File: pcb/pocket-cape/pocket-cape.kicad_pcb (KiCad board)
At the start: 4 copper layers, 49 x 32.1 mm, 27 parts, among them J1 Sync1, J10 Display, J11 USB1, J2 12..16V, J3 Sync2, J4 Sled, J5 Laser1, J6 PM1, J7 PM2, J8 Laser2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

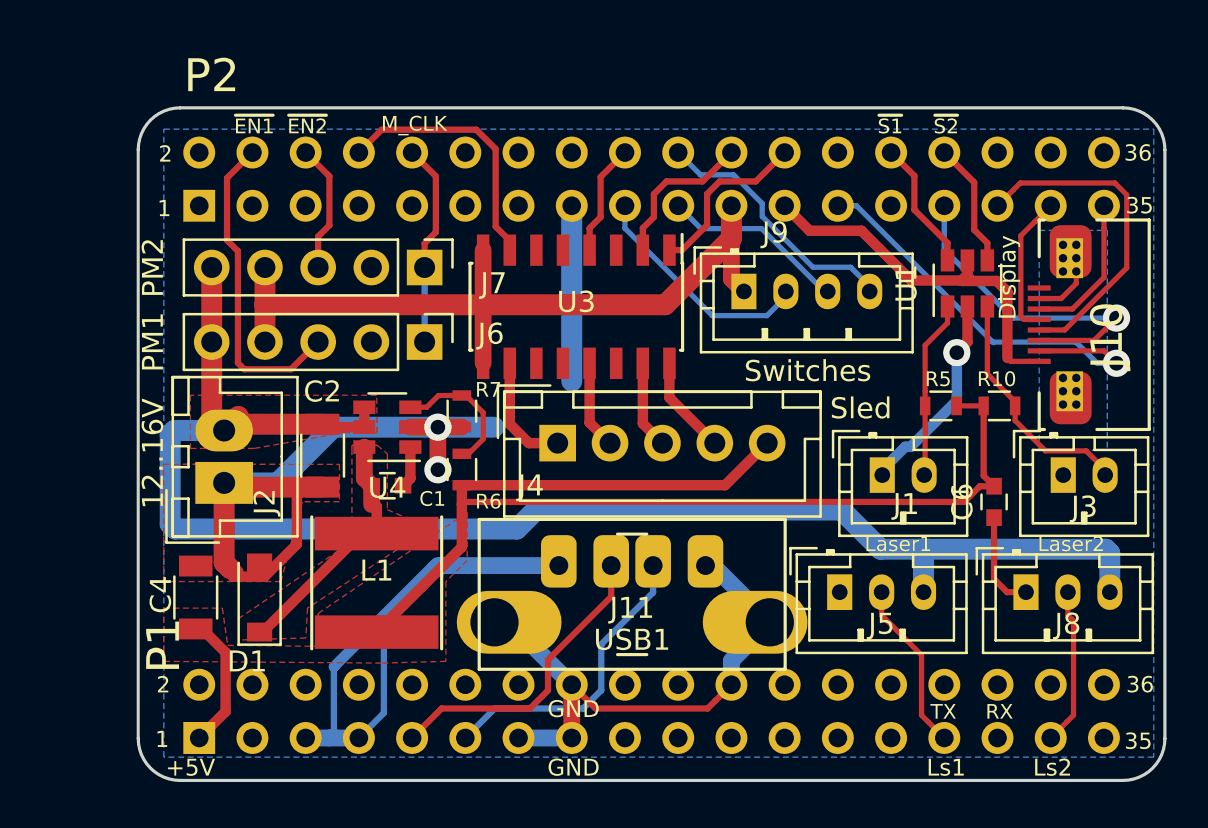
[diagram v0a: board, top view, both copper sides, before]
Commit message: Add a capacitor in the stepper driver vicinity.
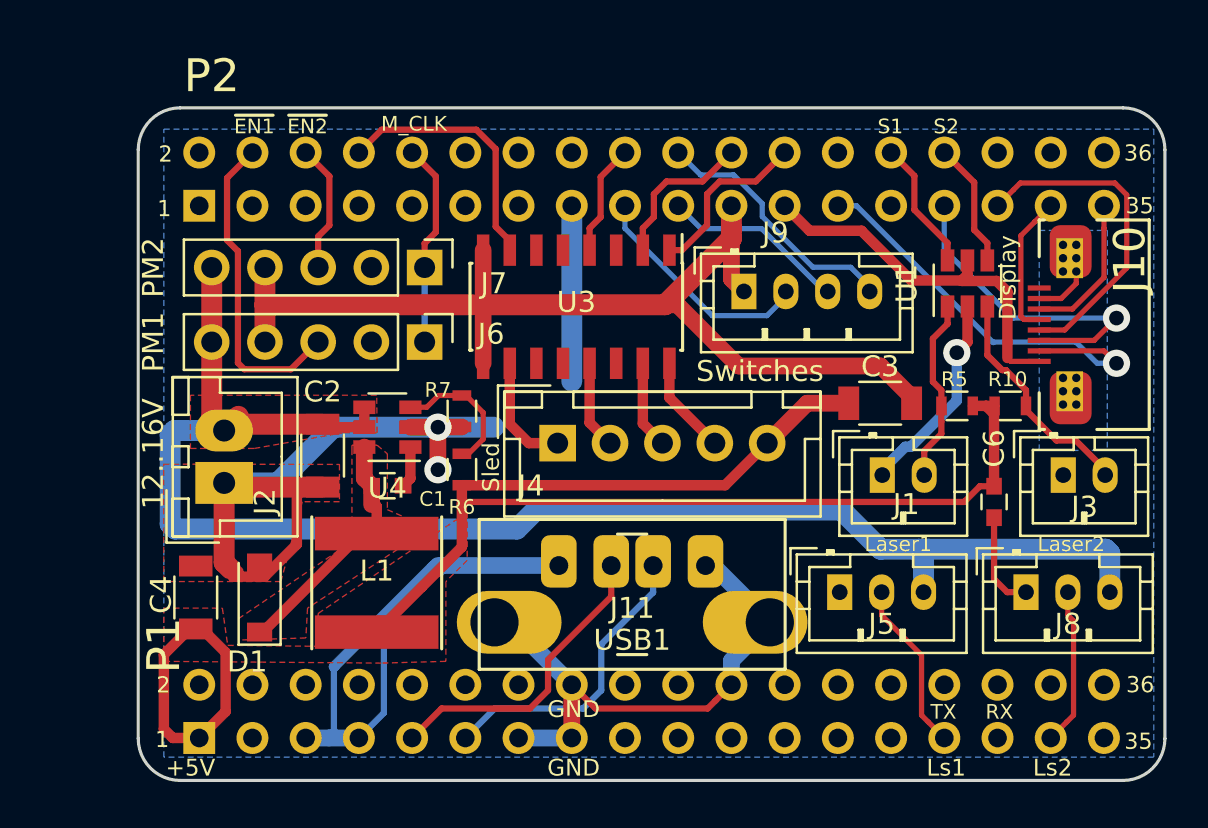
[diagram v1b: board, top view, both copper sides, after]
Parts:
- added C3: 22u, Capacitors_SMD:C_1206, F.Cu at (159.4, 103.0)
- moved R5 0.77 mm to (163.1, 103.1)
- moved REF*** 0.52 mm to (148.5, 97.8)
- moved R10 0.52 mm to (165.6, 103.1)
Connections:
- J10 pad 8: Net-(J10-Pad8) -> (no net)
- J6 pad 2: (no net) -> Net-(J6-Pad2)
- J7 pad 2: (no net) -> Net-(J7-Pad2)
- P1 pad 10: (no net) -> /(U1.B13)SPI0.MISO
- P1 pad 12: (no net) -> /(U1.B14)SPI0.MOSI
- P1 pad 14: Net-(P1-Pad14) -> (no net)
- P1 pad 17: (no net) -> /(U1.B9)VREF-
- P1 pad 18: (no net) -> /(U1.B7)VREF+
- P1 pad 19: (no net) -> /(U1.A8)AIN0~1.8V
- P1 pad 2: (no net) -> /(U1.F2)AIN6~3.3V
- P1 pad 20: (no net) -> /(U1.B4)PRU-0.16
- P1 pad 21: (no net) -> /(U1.B8)AIN1~1.8V
- P1 pad 23: (no net) -> /(U1.B6)AIN2~1.8V
- P1 pad 24: Net-(P1-Pad24) -> (no net)
- P1 pad 25: (no net) -> /(U1.C6)AIN3~1.8V
- P1 pad 26: (no net) -> /(U1.B10)I2C2.SDA
- P1 pad 27: (no net) -> /(U1.C7)AIN4~1.8V
- P1 pad 28: (no net) -> /(U1.A10)I2C2.SCL
- P1 pad 3: (no net) -> /(U1.M14)USB1.DRVVBUS
- P1 pad 30: (no net) -> /(U1.B12)UART0.TX
- P1 pad 31: (no net) -> /(U1.A3)PRU-0.4
- P1 pad 32: (no net) -> /(U1.A12)UART0.RX
- P1 pad 34: (no net) -> /(U1.R5)GPIO-0.26
- P1 pad 35: (no net) -> /(U1.F1)
- P1 pad 36: (no net) -> /(U1.A1)PWM0A
- P1 pad 4: (no net) -> /(U1.E1)
- P1 pad 6: (no net) -> /(U1.A14)SPI0.CS
- P1 pad 8: (no net) -> /(U1.A13)SPI0.CLK
- P2 pad 1: (no net) -> /(U1.P12)PWM1A
- P2 pad 11: (no net) -> /(U1.A11)I2C1.SDA
- P2 pad 12: (no net) -> /(U1.T11)PWR.BTN
- P2 pad 13: (no net) -> SYS_5V
- P2 pad 14: (no net) -> VIN.BAT
- P2 pad 16: (no net) -> /BAT.TEMP
- P2 pad 2: (no net) -> /(U1.T16)
- P2 pad 26: (no net) -> /(U1.R11)RESET#
- P2 pad 27: (no net) -> /(U1.C12)SPI1.MISO
- P2 pad 3: (no net) -> /(U1.P5)GPIO-0.23
- P2 pad 32: (no net) -> /(U1.B2)PRU-0.2
- P2 pad 34: (no net) -> /(U1.B3)PRU-0.5
- P2 pad 36: (no net) -> /(U1.N13)AIN7~1.8V
- P2 pad 5: (no net) -> /(U1.P15)UART4.RX
- P2 pad 7: (no net) -> /(U1.R16)UART4.TX
- P2 pad 9: (no net) -> /(U1.B11)I2C1.SCL
- U3 pad 11: Net-(U3-Pad11) -> (no net)
- U3 pad 12: Net-(U3-Pad12) -> (no net)
- U3 pad 14: Net-(U3-Pad14) -> (no net)
- U3 pad 3: Net-(U3-Pad3) -> (no net)
- U3 pad 5: Net-(U3-Pad5) -> (no net)
- U3 pad 6: Net-(U3-Pad6) -> (no net)
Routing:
- net GND: track 127.6 -> 141.8 mm
- net VDD_5V: track 64.3 -> 76.1 mm
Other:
- net class Default: clearance 0.18 -> 0.4
- rule trace_clearance: 0.18 -> 0.4
- board text added: "S1"
- board text added: "S2"
- board text removed: "~S1"
- board text removed: "~S2"

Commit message: Improve silkscreen.
o Label signals directly on header for easier measurements.
o Arrange partially obstructed component labels.
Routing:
- net +12V: track 75.3 -> 83.3 mm
- net GND: track 141.8 -> 145.3 mm
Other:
- board text added: "3.3V"
- board text added: "B1"
- board text added: "B2"
- board text added: "B3"
- board text added: "CLK"
- board text added: "DC"
- board text added: "HS1"
- board text added: "HS2"
- board text added: "MOSI"
- board text added: "RST"
- board text added: "~CS"
- board text removed: "S1"
- board text removed: "S2"
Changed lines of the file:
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@@
   (general
     (thickness 1.6)
-    (drawings 443)
-    (tracks 316)
+    (drawings 453)
+    (tracks 320)
     (zones 0)
     (modules 28)
@@
   )
   (setup
-    (last_trace_width 0.5)
+    (last_trace_width 1)
     (user_trace_width 0.25)
     (user_trace_width 0.3)
@@
     (pad_to_mask_clearance 0.0254)
     (aux_axis_origin 0 0)
-    (visible_elements FFFFEF7F)
+    (visible_elements FFFDEF7F)
     (pcbplotparams
       (layerselection 0x010fc_fffffff9)
@@
       (effects (font (size 0.7 0.7) (thickness 0.15)))
     )
-    (fp_text value C (at 0 1.5 180) (layer F.Fab)
+    (fp_text value C (at 0 0 180) (layer F.Fab)
       (effects (font (size 1 1) (thickness 0.15)))
     )
@@
       (effects (font (size 1 1) (thickness 0.15)))
     )
-    (fp_text value 10u (at 0 2 270) (layer F.Fab)
+    (fp_text value 10u (at 0.037 -0.042 270) (layer F.Fab)
       (effects (font (size 1 1) (thickness 0.15)))
     )
@@
     (fp_line (start 1.6 0.8) (end -1.6 0.8) (layer F.Fab) (width 0.1))
     (fp_line (start -1.6 0.8) (end -1.6 -0.8) (layer F.Fab) (width 0.1))
-    (fp_text user %R (at 0 -1.75 270) (layer F.Fab)
+    (fp_text user %R (at 2.577 0.212 270) (layer F.Fab)
       (effects (font (size 1 1) (thickness 0.15)))
     )
@@
       (effects (font (size 1 1) (thickness 0.15)))
     )
-    (fp_text value 22u (at 0 2 90) (layer F.Fab)
+    (fp_text value 22u (at 0 0 90) (layer F.Fab)
       (effects (font (size 1 1) (thickness 0.15)))
     )
@@
       (effects (font (size 1 1) (thickness 0.15)))
     )
-    (fp_text value D (at 0 2.1 90) (layer F.Fab)
+    (fp_text value D (at 0.762 0.127 90) (layer F.Fab)
       (effects (font (size 1 1) (thickness 0.15)))
     )
-    (fp_text user %R (at 0 -2 90) (layer F.Fab)
+    (fp_text user %R (at -1.27 1.651 90) (layer F.Fab)
       (effects (font (size 1 1) (thickness 0.15)))
     )
@@
       (effects (font (size 0.7 0.7) (thickness 0.15)))
     )
-    (fp_text value R (at 0 1.5 90) (layer F.Fab)
+    (fp_text value R (at 0.115 1.397 90) (layer F.Fab)
       (effects (font (size 1 1) (thickness 0.15)))
     )
@@
       (effects (font (size 0.7 0.7) (thickness 0.15)))
     )
-    (fp_text value R (at 0 1.5 270) (layer F.Fab)
+    (fp_text value R (at -0.127 -1.397 270) (layer F.Fab)
       (effects (font (size 1 1) (thickness 0.15)))
     )
-    (fp_text user %R (at 0.065999 2.3475 270) (layer F.Fab)
+    (fp_text user %R (at 0 0 270) (layer F.Fab)
       (effects (font (size 0.4 0.4) (thickness 0.075)))
     )
@@
     (tags SOT-23-6)
     (attr smd)
-    (fp_text reference U4 (at 0 -2.9 180) (layer F.SilkS)
+    (fp_text reference U4 (at 0.127 2.159 180) (layer F.SilkS)
       (effects (font (size 1 1) (thickness 0.15)))
     )
@@
       (effects (font (size 0.7 0.7) (thickness 0.12)))
     )
-    (fp_text value 100k (at 0 1.5) (layer F.Fab)
+    (fp_text value 100k (at -0.266 -1.27) (layer F.Fab)
       (effects (font (size 1 1) (thickness 0.15)))
     )
@@
       (effects (font (size 0.7 0.7) (thickness 0.12)))
     )
-    (fp_text value 100k (at 0.762 1.143 180) (layer F.Fab)
+    (fp_text value 100k (at -1.131 1.27 180) (layer F.Fab)
       (effects (font (size 1 1) (thickness 0.15)))
     )
@@
       (effects (font (size 1 1) (thickness 0.15)))
     )
-    (fp_text value 4u7 (at 0 4.5 270) (layer F.Fab)
+    (fp_text value 4u7 (at 0.19 -2.159 270) (layer F.Fab)
       (effects (font (size 1 1) (thickness 0.15)))
     )
@@
       (effects (font (size 1 1) (thickness 0.15)))
     )
-    (fp_text value 100n (at 0 1.5 90) (layer F.Fab)
+    (fp_text value 100n (at 0.139 1.143 90) (layer F.Fab)
       (effects (font (size 1 1) (thickness 0.15)))
     )
-    (fp_text user %R (at 0 -1.5 90) (layer F.Fab)
+    (fp_text user %R (at 1.917 0.127 90) (layer F.Fab)
       (effects (font (size 1 1) (thickness 0.15)))
     )
@@
     (tags "SOIC 1.27")
     (attr smd)
-    (fp_text reference U3 (at -0.221 0) (layer F.SilkS)
+    (fp_text reference U3 (at -3.269 -6.223) (layer F.SilkS)
       (effects (font (size 1 1) (thickness 0.15)))
     )
@@
     (descr "JST PH series connector, B4B-PH-K, top entry type, through hole, Datasheet: http://www.jst-mfg.com/product/pdf/eng/ePH.pdf")
     (tags "connector jst ph")
-    (fp_text reference J9 (at 1.5 -2.8) (layer F.SilkS)
+    (fp_text reference J9 (at 5 1.8) (layer F.SilkS)
       (effects (font (size 1 1) (thickness 0.15)))
     )
@@
       (effects (font (size 1 1) (thickness 0.15)))
     )
-    (fp_text value Sync1 (at 1 3.8) (layer F.Fab)
+    (fp_text value Sync1 (at 1.143 2.413) (layer F.Fab)
       (effects (font (size 1 1) (thickness 0.15)))
     )
@@
       (effects (font (size 1 1) (thickness 0.15)))
     )
-    (fp_text value Sync2 (at 1 3.8) (layer F.Fab)
+    (fp_text value Sync2 (at 1.143 2.413) (layer F.Fab)
       (effects (font (size 1 1) (thickness 0.15)))
     )
@@
     (tags SOT-23-6)
     (attr smd)
-    (fp_text reference U1 (at 0 -2.9 90) (layer F.SilkS)
+    (fp_text reference U1 (at -2.794 1.143 180) (layer F.SilkS)
       (effects (font (size 1 1) (thickness 0.15)))
     )
-    (fp_text value 74LVC2G14GV (at 0 2.9 90) (layer F.Fab)
+    (fp_text value 74LVC2G14GV (at 1.905 -0.635 180) (layer F.Fab)
       (effects (font (size 1 1) (thickness 0.15)))
     )
@@
       (effects (font (size 1 1) (thickness 0.15)))
     )
-    (fp_text value 22u (at 0 2) (layer F.Fab)
+    (fp_text value 22u (at 0.103 0) (layer F.Fab)
       (effects (font (size 1 1) (thickness 0.15)))
     )
@@
     )
   )
+  (gr_text 3.3V (at 142.367 117.729) (layer F.SilkS)
+    (effects (font (size 0.6 0.6) (thickness 0.12)))
+  )
+  (gr_text 3.3V (at 154.94 92.329) (layer F.SilkS)
+    (effects (font (size 0.6 0.6) (thickness 0.12)))
+  )
+  (gr_text "MOSI\n\n" (at 157.48 92.964) (layer F.SilkS)
+    (effects (font (size 0.7 0.7) (thickness 0.12)))
+  )
+  (gr_text CLK (at 162.56 92.329) (layer F.SilkS)
+    (effects (font (size 0.7 0.7) (thickness 0.12)))
+  )
+  (gr_text ~CS (at 164.973 92.456) (layer F.SilkS)
+    (effects (font (size 0.6 0.6) (thickness 0.12)))
+  )
+  (gr_text DC (at 167.513 92.329) (layer F.SilkS)
+    (effects (font (size 0.7 0.7) (thickness 0.12)))
+  )
+  (gr_text RST (at 170.053 92.329) (layer F.SilkS)
+    (effects (font (size 0.7 0.7) (thickness 0.12)))
+  )
+  (gr_text B1 (at 147.193 92.456) (layer F.SilkS)
+    (effects (font (size 0.7 0.7) (thickness 0.15)))
+  )
+  (gr_text B2 (at 149.86 92.329) (layer F.SilkS)
+    (effects (font (size 0.7 0.7) (thickness 0.15)))
+  )
+  (gr_text B3 (at 149.86 89.789) (layer F.SilkS)
+    (effects (font (size 0.7 0.7) (thickness 0.15)))
+  )
   (gr_arc (start 171 90.9) (end 173 90.9) (angle -90) (layer Edge.Cuts) (width 0.15))
   (gr_arc (start 171 119) (end 171 121) (angle -90) (layer Edge.Cuts) (width 0.15))
@@
     (effects (font (size 0.8 0.8) (thickness 0.15)))
   )
-  (gr_text S1 (at 159.893 89.789) (layer F.SilkS)
+  (gr_text HS1 (at 159.893 89.789) (layer F.SilkS)
     (effects (font (size 0.7 0.7) (thickness 0.15)))
   )
-  (gr_text S2 (at 162.56 89.789) (layer F.SilkS)
+  (gr_text HS2 (at 162.56 89.789) (layer F.SilkS)
     (effects (font (size 0.7 0.7) (thickness 0.15)))
   )
@@
     (effects (font (size 0.0475 0.0475) (thickness 0.004)) (justify left bottom))
   )
+  (segment (start 130.048 96.52) (end 130.048 100.076) (width 1) (layer Bottom) (net 1))
   (segment (start 152.654 101.219) (end 159.431 101.219) (width 0.8) (layer Top) (net 1))
   (segment (start 159.431 101.219) (end 160.909 102.697) (width 0.8) (layer Top) (net 1))
@@
   (segment (start 136.99 105.09) (end 136.99 106.584) (width 0.5) (layer Top) (net 4))
   (segment (start 136.99 106.584) (end 136.64 106.934) (width 0.5) (layer Top) (net 4))
+  (segment (start 127.508 100.076) (end 127.508 103.708) (width 1) (layer Bottom) (net 5))
+  (segment (start 127.508 103.708) (end 128.1 104.3) (width 1) (layer Bottom) (net 5))
+  (segment (start 127.508 96.52) (end 127.508 100.076) (width 1) (layer Bottom) (net 5))
   (segment (start 161.48 110.164) (end 161.680001 109.963999) (width 1) (layer Bottom) (net 5))
   (segment (start 161.680001 109.963999) (end 170.169999 109.963999) (width 1) (layer Bottom) (net 5))

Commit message: Connect to more local GND on Hsync stabilizing cap.
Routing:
- net GND: track 145.3 -> 144.8 mm
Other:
- net class Default: clearance 0.4 -> 0.18
- rule trace_clearance: 0.4 -> 0.18
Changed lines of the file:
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@@
     (thickness 1.6)
     (drawings 453)
-    (tracks 320)
+    (tracks 319)
     (zones 0)
     (modules 28)
@@
   )
   (setup
-    (last_trace_width 1)
+    (last_trace_width 0.5)
     (user_trace_width 0.25)
     (user_trace_width 0.3)
@@
     (user_trace_width 1)
     (user_trace_width 2)
-    (trace_clearance 0.4)
+    (trace_clearance 0.18)
     (zone_clearance 0.5)
     (zone_45_only no)
@@
   (net 76 "/(U1.P12)PWM1A")
   (net_class Default "This is the default net class."
-    (clearance 0.4)
+    (clearance 0.18)
     (trace_width 0.25)
     (via_dia 1.3)
@@
     (effects (font (size 0.0475 0.0475) (thickness 0.004)) (justify left bottom))
   )
+  (segment (start 164.846 108.458) (end 166.116 108.458) (width 0.5) (layer Top) (net 1))
+  (segment (start 166.116 108.458) (end 168.148 106.426) (width 0.5) (layer Top) (net 1))
   (segment (start 130.048 96.52) (end 130.048 100.076) (width 1) (layer Bottom) (net 1))
   (segment (start 152.654 101.219) (end 159.431 101.219) (width 0.8) (layer Top) (net 1))
@@
   (segment (start 151.179099 117.565601) (end 151.549101 117.195599) (width 0.3) (layer Top) (net 1))
   (segment (start 151.549101 117.195599) (end 152.3111 116.4336) (width 0.3) (layer Top) (net 1))
-  (segment (start 164.846 108.458) (end 164.846 111.39) (width 0.3) (layer Top) (net 1))
-  (segment (start 164.846 111.39) (end 165.47 112.014) (width 0.3) (layer Top) (net 1))
-  (segment (start 165.47 112.014) (end 166.37 112.014) (width 0.3) (layer Top) (net 1))
   (segment (start 163.068 100.584) (end 163.068 102.87) (width 0.5) (layer Bottom) (net 1))
   (segment (start 163.068 102.87) (end 160.862 105.076) (width 0.5) (layer Bottom) (net 1))
